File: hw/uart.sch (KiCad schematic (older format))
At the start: 0 parts

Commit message: hw: add MAX3109 symbol
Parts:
- added C?: 0.1, symbol C
- added C?: 1.0, symbol C
- added DD?: MAX3109, Housings_DFN_QFN:QFN-32-1EP_5x5mm_Pitch0.5mm, symbol MAX3109
- added R? (x2): 10k, symbol R
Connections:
- new net: DD?.1 (~RST), R?.1
- new net: C?.1, DD?.31 (V18)
- new net +3.3VP: C?.1, DD?.25 (Vext), DD?.30 (LDOEN), DD?.32 (Vcc), DD?.8 (Vl), DD?.9 (SPI/~I2C), R?.2, R?.2
- new net GND: C?.2, C?.2, DD?.10 (DGND), DD?.29 (AGND), DD?.33 (AGND)
- new net RPI_GPCLK0: DD?.26 (XIN)
- new net RPI_SPI0_MISO: DD?.2 (MISO/SDA)
- new net RPI_SPI0_MOSI: DD?.6 (MOSI/A1)
- new net RPI_SPI0_SCLK: DD?.3 (SCLK/SCL)
- new net ~RPI_SPI0_CE0: DD?.5 (~CS~/A0)
- new net ~SER_IRQ: DD?.7 (~IRQ), R?.1
- no-connect marks 0 -> 1
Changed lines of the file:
@@
 Comment4 ""
 $EndDescr
+$Comp
+L MAX3109 DD?
+U 1 1 5AB1B0A7
+P 4400 4900
+F 0 "DD?" H 3900 6100 60  0000 C CNN
+F 1 "MAX3109" H 4400 3700 60  0000 C CNN
+F 2 "Housings_DFN_QFN:QFN-32-1EP_5x5mm_Pitch0.5mm" H 4400 4600 60  0001 C CNN
+F 3 "" H 4400 4600 60  0001 C CNN
+	1    4400 4900
+	1    0    0    -1
+$EndComp
+$Comp
+L +3.3VP #PWR013
+U 1 1 5AB1B260
+P 3250 5400
+F 0 "#PWR013" H 3400 5350 50  0001 C CNN
+F 1 "+3.3VP" H 3250 5500 50  0000 C CNN
+F 2 "" H 3250 5400 50  0001 C CNN
+F 3 "" H 3250 5400 50  0001 C CNN
+	1    3250 5400
+	1    0    0    -1
+$EndComp
+$Comp
+L GND #PWR014
+U 1 1 5AB1B2D7
+P 3500 6500
+F 0 "#PWR014" H 3500 6250 50  0001 C CNN
+F 1 "GND" H 3500 6350 50  0000 C CNN
+F 2 "" H 3500 6500 50  0001 C CNN
+F 3 "" H 3500 6500 50  0001 C CNN
+	1    3500 6500
+	1    0    0    -1
+$EndComp
+NoConn ~ 3600 5150
+Text GLabel 2950 5050 0    60   Input ~ 0
+RPI_GPCLK0
+Wire Wire Line
+	2950 5050 3600 5050
+$Comp
+L C C?
+U 1 1 5AB1B470
+P 3250 6150
+F 0 "C?" H 3275 6250 50  0000 L CNN
+F 1 "0.1" H 3275 6050 50  0000 L CNN
+F 2 "" H 3288 6000 50  0001 C CNN
+F 3 "" H 3250 6150 50  0001 C CNN
+	1    3250 6150
+	1    0    0    -1
+$EndComp
+$Comp
+L C C?
+U 1 1 5AB1B4D8
+P 3500 6150
+F 0 "C?" H 3525 6250 50  0000 L CNN
+F 1 "1.0" H 3525 6050 50  0000 L CNN
+F 2 "" H 3538 6000 50  0001 C CNN
+F 3 "" H 3500 6150 50  0001 C CNN
+	1    3500 6150
+	1    0    0    -1
+$EndComp
+Wire Wire Line
+	3600 5900 3500 5900
+Wire Wire Line
+	3500 5900 3500 6000
+Wire Wire Line
+	3600 5500 3250 5500
+Wire Wire Line
+	3250 5400 3250 6000
+Wire Wire Line
+	3250 5600 3600 5600
+Connection ~ 3250 5600
+Wire Wire Line
+	3600 5700 3250 5700
+Connection ~ 3250 5700
+Connection ~ 3250 5500
+Wire Wire Line
+	3500 6300 3500 6500
+Wire Wire Line
+	3500 6400 3250 6400
+Wire Wire Line
+	3250 6400 3250 6300
+Connection ~ 3500 6400
+$Comp
+L +3.3VP #PWR015
+U 1 1 5AB1B914
+P 2900 4750
+F 0 "#PWR015" H 3050 4700 50  0001 C CNN
+F 1 "+3.3VP" H 2900 4850 50  0000 C CNN
+F 2 "" H 2900 4750 50  0001 C CNN
+F 3 "" H 2900 4750 50  0001 C CNN
+	1    2900 4750
+	0    -1   -1   0
+$EndComp
+$Comp
+L R R?
+U 1 1 5AB1B9A3
+P 3250 4550
+F 0 "R?" V 3330 4550 50  0000 C CNN
+F 1 "10k" V 3250 4550 50  0000 C CNN
+F 2 "" V 3180 4550 50  0001 C CNN
+F 3 "" H 3250 4550 50  0001 C CNN
+	1    3250 4550
+	0    1    1    0
+$EndComp
+Wire Wire Line
+	2900 4750 3600 4750
+Wire Wire Line
+	3600 4650 3500 4650
+Wire Wire Line
+	3500 4650 3500 4750
+Connection ~ 3500 4750
+Wire Wire Line
+	3000 4750 3000 4550
+Wire Wire Line
+	3000 4550 3100 4550
+Connection ~ 3000 4750
+Text GLabel 2950 4450 0    60   Output ~ 0
+~SER_IRQ
+Text GLabel 2950 4350 0    60   Input ~ 0
+~RPI_SPI0_CE0
+Text GLabel 2950 4250 0    60   Input ~ 0
+RPI_SPI0_SCLK
+Text GLabel 2950 4150 0    60   Input ~ 0
+RPI_SPI0_MOSI
+Text GLabel 2950 4050 0    60   Output ~ 0
+RPI_SPI0_MISO
+Wire Wire Line
+	2950 4050 3600 4050
+Wire Wire Line
+	3600 4150 2950 4150
+Wire Wire Line
+	2950 4250 3600 4250
+Wire Wire Line
+	3600 4350 2950 4350
+Wire Wire Line
+	2950 4450 3600 4450
+Wire Wire Line
+	3400 4550 3500 4550
+Wire Wire Line
+	3500 4550 3500 4450
+Connection ~ 3500 4450
+$Comp
+L GND #PWR016
+U 1 1 5AB1C686
+P 5300 6050
+F 0 "#PWR016" H 5300 5800 50  0001 C CNN
+F 1 "GND" H 5300 5900 50  0000 C CNN
+F 2 "" H 5300 6050 50  0001 C CNN
+F 3 "" H 5300 6050 50  0001 C CNN
+	1    5300 6050
+	1    0    0    -1
+$EndComp
+Wire Wire Line
+	5200 5700 5300 5700
+Wire Wire Line
+	5300 5700 5300 6050
+Wire Wire Line
+	5200 5800 5300 5800
+Connection ~ 5300 5800
+Wire Wire Line
+	5200 5900 5300 5900
+Connection ~ 5300 5900
+$Comp
+L R R?
+U 1 1 5AB1D90A
+P 3500 3650
+F 0 "R?" V 3580 3650 50  0000 C CNN
+F 1 "10k" V 3500 3650 50  0000 C CNN
+F 2 "" V 3430 3650 50  0001 C CNN
+F 3 "" H 3500 3650 50  0001 C CNN
+	1    3500 3650
+	-1   0    0    1
+$EndComp
+$Comp
+L +3.3VP #PWR017
+U 1 1 5AB1D959
+P 3500 3400
+F 0 "#PWR017" H 3650 3350 50  0001 C CNN
+F 1 "+3.3VP" H 3500 3500 50  0000 C CNN
+F 2 "" H 3500 3400 50  0001 C CNN
+F 3 "" H 3500 3400 50  0001 C CNN
+	1    3500 3400
+	1    0    0    -1
+$EndComp
+Wire Wire Line
+	3600 3900 3500 3900
+Wire Wire Line
+	3500 3900 3500 3800
+Wire Wire Line
+	3500 3500 3500 3400
 $EndSCHEMATC

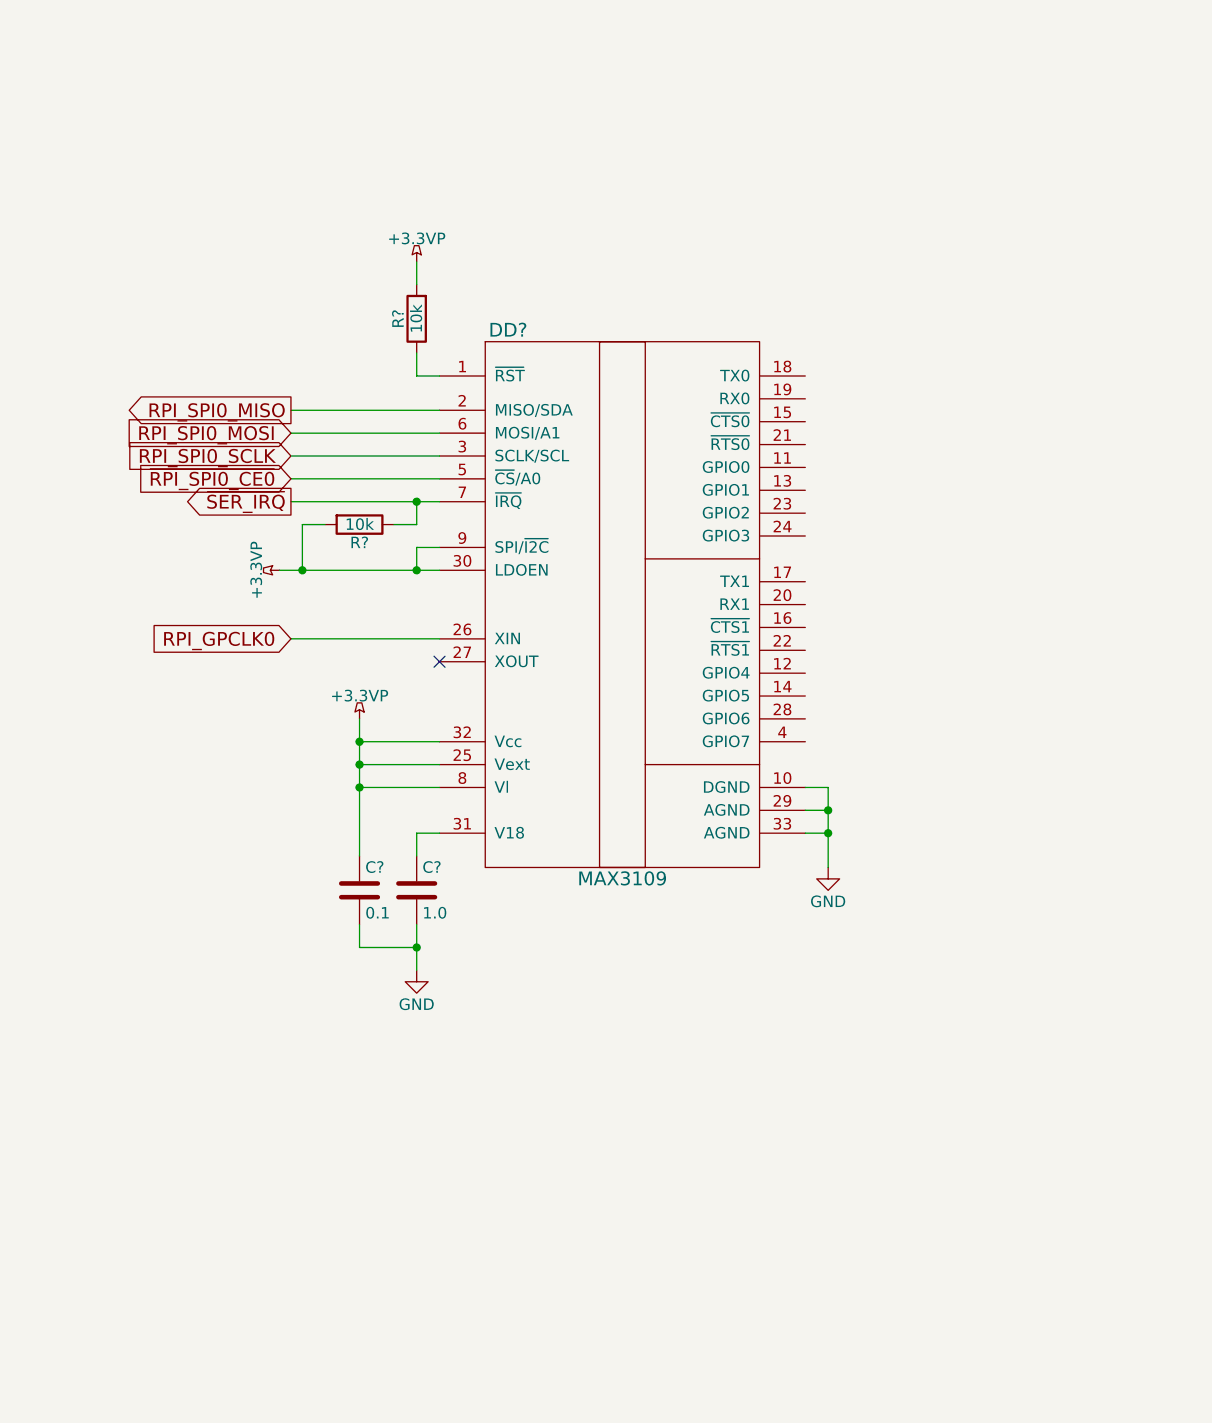
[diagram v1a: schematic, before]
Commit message: hw: add uart conns
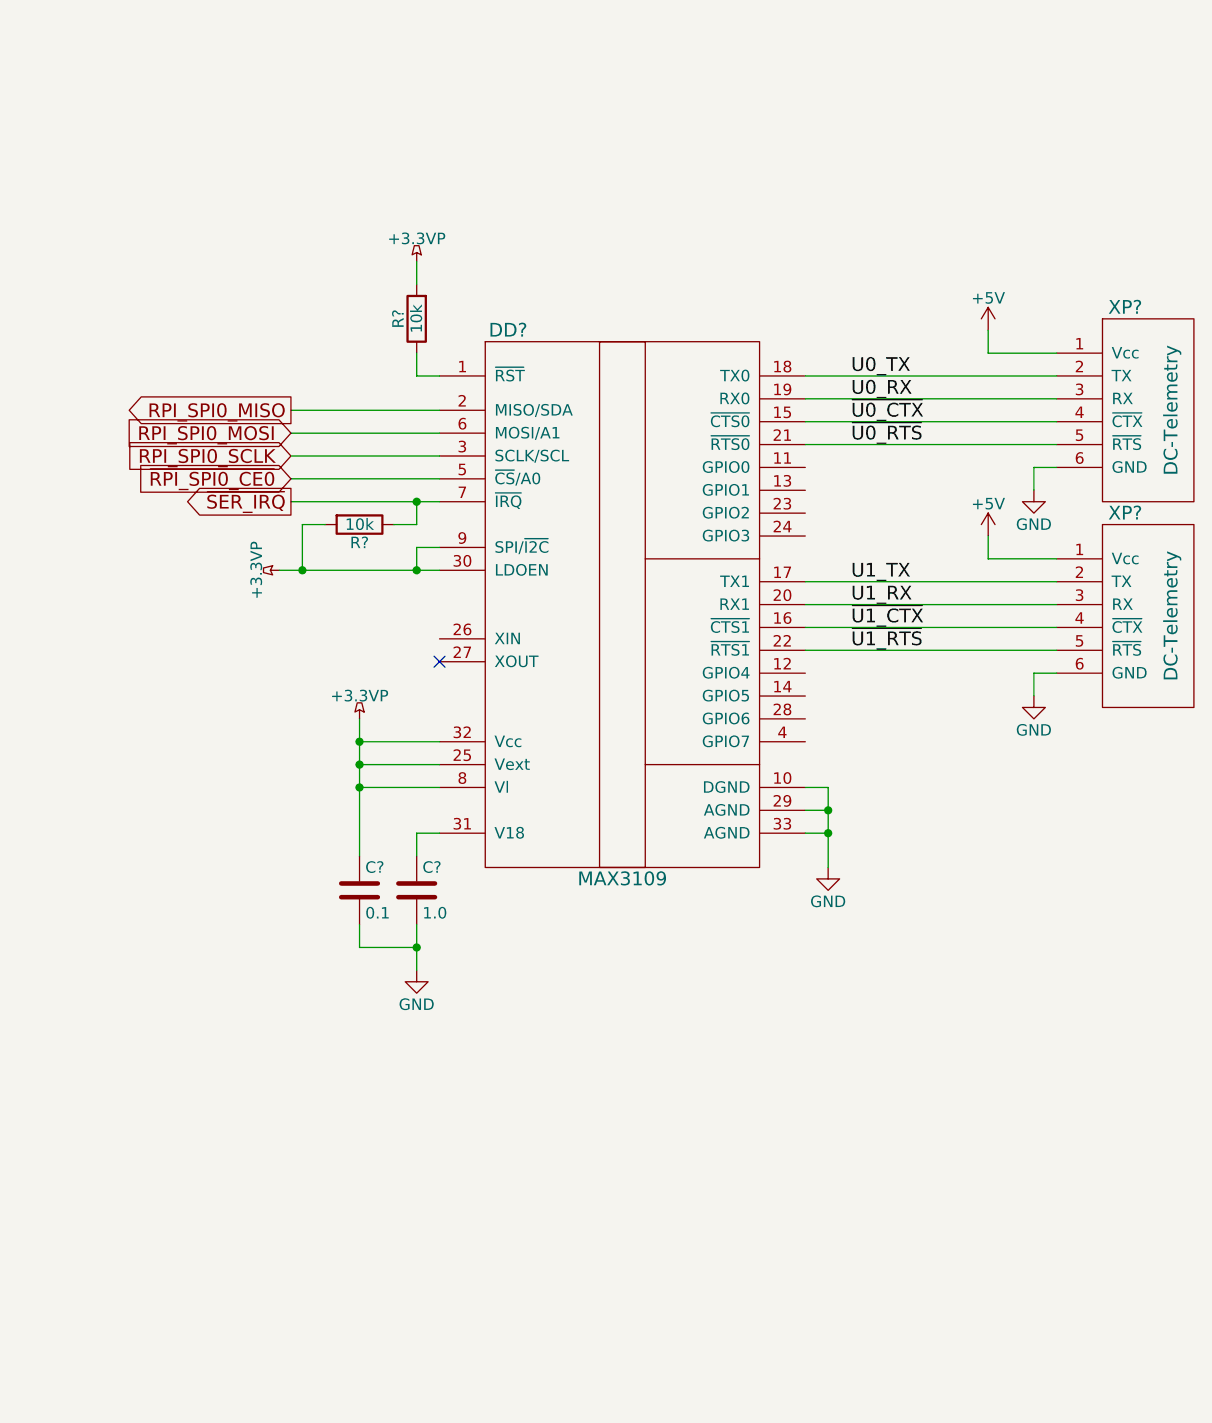
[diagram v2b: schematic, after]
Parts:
- added XP? (x2): DC-Telemetry, symbol DC-Telemetry
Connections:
- net GND: now also XP?.6 (GND), XP?.6 (GND)
- net ~U0_CTX: now reaches DD?.15 (~CTS0)
- net ~U0_CTX: now also XP?.4 (~CTX)
- net ~U1_CTX: now reaches DD?.16 (~CTS1)
- net ~U1_CTX: now also XP?.4 (~CTX)
- net U1_TX: now reaches DD?.17 (TX1)
- net U1_TX: now also XP?.2 (TX)
- net U0_TX: now reaches DD?.18 (TX0)
- net U0_TX: now also XP?.2 (TX)
- net U0_RX: now reaches DD?.19 (RX0)
- net U0_RX: now also XP?.3 (RX)
- net U1_RX: now reaches DD?.20 (RX1)
- net U1_RX: now also XP?.3 (RX)
- net ~U0_RTS: now reaches DD?.21 (~RTS0)
- net ~U0_RTS: now also XP?.5 (~RTS)
- net ~U1_RTS: now reaches DD?.22 (~RTS1)
- net ~U1_RTS: now also XP?.5 (~RTS)
- net RPI_GPCLK0: no longer names the net of DD?.26 (XIN)
- new net +5V: XP?.1 (Vcc), XP?.1 (Vcc)
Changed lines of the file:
@@
 LIBS:rpi_con
 LIBS:ic
+LIBS:dronecode_con
 LIBS:obc-drone-hat-cache
 EELAYER 25 0
@@
 $EndComp
 NoConn ~ 3600 5150
-Text GLabel 2950 5050 0    60   Input ~ 0
-RPI_GPCLK0
-Wire Wire Line
-	2950 5050 3600 5050
 $Comp
 L C C?
@@
 	3600 5500 3250 5500
 Wire Wire Line
-	3250 5400 3250 6000
+	3250 5400 3250 5500
+Wire Wire Line
+	3250 5500 3250 5600
+Wire Wire Line
+	3250 5600 3250 5700
+Wire Wire Line
+	3250 5700 3250 6000
 Wire Wire Line
 	3250 5600 3600 5600
@@
 Connection ~ 3250 5500
 Wire Wire Line
-	3500 6300 3500 6500
+	3500 6300 3500 6400
+Wire Wire Line
+	3500 6400 3500 6500
 Wire Wire Line
 	3500 6400 3250 6400
@@
 $EndComp
 Wire Wire Line
-	2900 4750 3600 4750
+	2900 4750 3000 4750
+Wire Wire Line
+	3000 4750 3500 4750
+Wire Wire Line
+	3500 4750 3600 4750
 Wire Wire Line
 	3600 4650 3500 4650
@@
 	3600 4350 2950 4350
 Wire Wire Line
-	2950 4450 3600 4450
+	2950 4450 3500 4450
+Wire Wire Line
+	3500 4450 3600 4450
 Wire Wire Line
 	3400 4550 3500 4550
@@
 L GND #PWR016
 U 1 1 5AB1C686
-P 5300 6050
-F 0 "#PWR016" H 5300 5800 50  0001 C CNN
-F 1 "GND" H 5300 5900 50  0000 C CNN
-F 2 "" H 5300 6050 50  0001 C CNN
-F 3 "" H 5300 6050 50  0001 C CNN
-	1    5300 6050
+P 6200 4400
+F 0 "#PWR016" H 6200 4150 50  0001 C CNN
+F 1 "GND" H 6200 4250 50  0000 C CNN
+F 2 "" H 6200 4400 50  0001 C CNN
+F 3 "" H 6200 4400 50  0001 C CNN
+	1    6200 4400
 	1    0    0    -1
 $EndComp
@@
 	5200 5700 5300 5700
 Wire Wire Line
-	5300 5700 5300 6050
+	5300 5700 5300 5800
+Wire Wire Line
+	5300 5800 5300 5900
+Wire Wire Line
+	5300 5900 5300 6050
 Wire Wire Line
 	5200 5800 5300 5800
@@
 Wire Wire Line
 	3500 3500 3500 3400
+$Comp
+L DC-Telemetry XP?
+U 1 1 5AB2FA79
+P 6700 4050
+F 0 "XP?" H 6600 4500 60  0000 C CNN
+F 1 "DC-Telemetry" V 6800 4050 60  0000 C CNN
+F 2 "" H 6700 4050 60  0001 C CNN
+F 3 "" H 6700 4050 60  0001 C CNN
+	1    6700 4050
+	1    0    0    -1
+$EndComp
+$Comp
+L DC-Telemetry XP?
+U 1 1 5AB2FFF0
+P 6700 4950
+F 0 "XP?" H 6600 5400 60  0000 C CNN
+F 1 "DC-Telemetry" V 6800 4950 60  0000 C CNN
+F 2 "" H 6700 4950 60  0001 C CNN
+F 3 "" H 6700 4950 60  0001 C CNN
+	1    6700 4950
+	1    0    0    -1
+$EndComp
+Wire Wire Line
+	5200 3900 6300 3900
+Wire Wire Line
+	5200 4000 6300 4000
+Wire Wire Line
+	5200 4800 6300 4800
+Wire Wire Line
+	6300 4900 5200 4900
+Wire Wire Line
+	5200 4100 6300 4100
+Wire Wire Line
+	5200 4200 6300 4200
+Wire Wire Line
+	5200 5000 6300 5000
+Wire Wire Line
+	6300 5100 5200 5100
+$Comp
+L +5V #PWR?
+U 1 1 5AB3063A
+P 6000 3700
+F 0 "#PWR?" H 6000 3550 50  0001 C CNN
+F 1 "+5V" H 6000 3840 50  0000 C CNN
+F 2 "" H 6000 3700 50  0001 C CNN
+F 3 "" H 6000 3700 50  0001 C CNN
+	1    6000 3700
+	1    0    0    -1
+$EndComp
+Wire Wire Line
+	6300 4300 6200 4300
+Wire Wire Line
+	6200 4300 6200 4400
+$Comp
+L GND #PWR?
+U 1 1 5AB30BD8
+P 5300 6050
+F 0 "#PWR?" H 5300 5800 50  0001 C CNN
+F 1 "GND" H 5300 5900 50  0000 C CNN
+F 2 "" H 5300 6050 50  0001 C CNN
+F 3 "" H 5300 6050 50  0001 C CNN
+	1    5300 6050
+	1    0    0    -1
+$EndComp
+$Comp
+L GND #PWR?
+U 1 1 5AB30BF8
+P 6200 5300
+F 0 "#PWR?" H 6200 5050 50  0001 C CNN
+F 1 "GND" H 6200 5150 50  0000 C CNN
+F 2 "" H 6200 5300 50  0001 C CNN
+F 3 "" H 6200 5300 50  0001 C CNN
+	1    6200 5300
+	1    0    0    -1
+$EndComp
+$Comp
+L +5V #PWR?
+U 1 1 5AB30E1E
+P 6000 4600
+F 0 "#PWR?" H 6000 4450 50  0001 C CNN
+F 1 "+5V" H 6000 4740 50  0000 C CNN
+F 2 "" H 6000 4600 50  0001 C CNN
+F 3 "" H 6000 4600 50  0001 C CNN
+	1    6000 4600
+	1    0    0    -1
+$EndComp
+Wire Wire Line
+	6300 5200 6200 5200
+Wire Wire Line
+	6200 5200 6200 5300
+Wire Wire Line
+	6300 4700 6000 4700
+Wire Wire Line
+	6000 4700 6000 4600
+Wire Wire Line
+	6300 3800 6000 3800
+Wire Wire Line
+	6000 3800 6000 3700
+Text Label 5400 3900 0    60   ~ 0
+U0_TX
+Text Label 5400 4000 0    60   ~ 0
+U0_RX
+Text Label 5400 4100 0    60   ~ 0
+~U0_CTX
+Text Label 5400 4200 0    60   ~ 0
+~U0_RTS
+Text Label 5400 4800 0    60   ~ 0
+U1_TX
+Text Label 5400 4900 0    60   ~ 0
+U1_RX
+Text Label 5400 5000 0    60   ~ 0
+~U1_CTX
+Text Label 5400 5100 0    60   ~ 0
+~U1_RTS
 $EndSCHEMATC

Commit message: hw: add fallback clk source
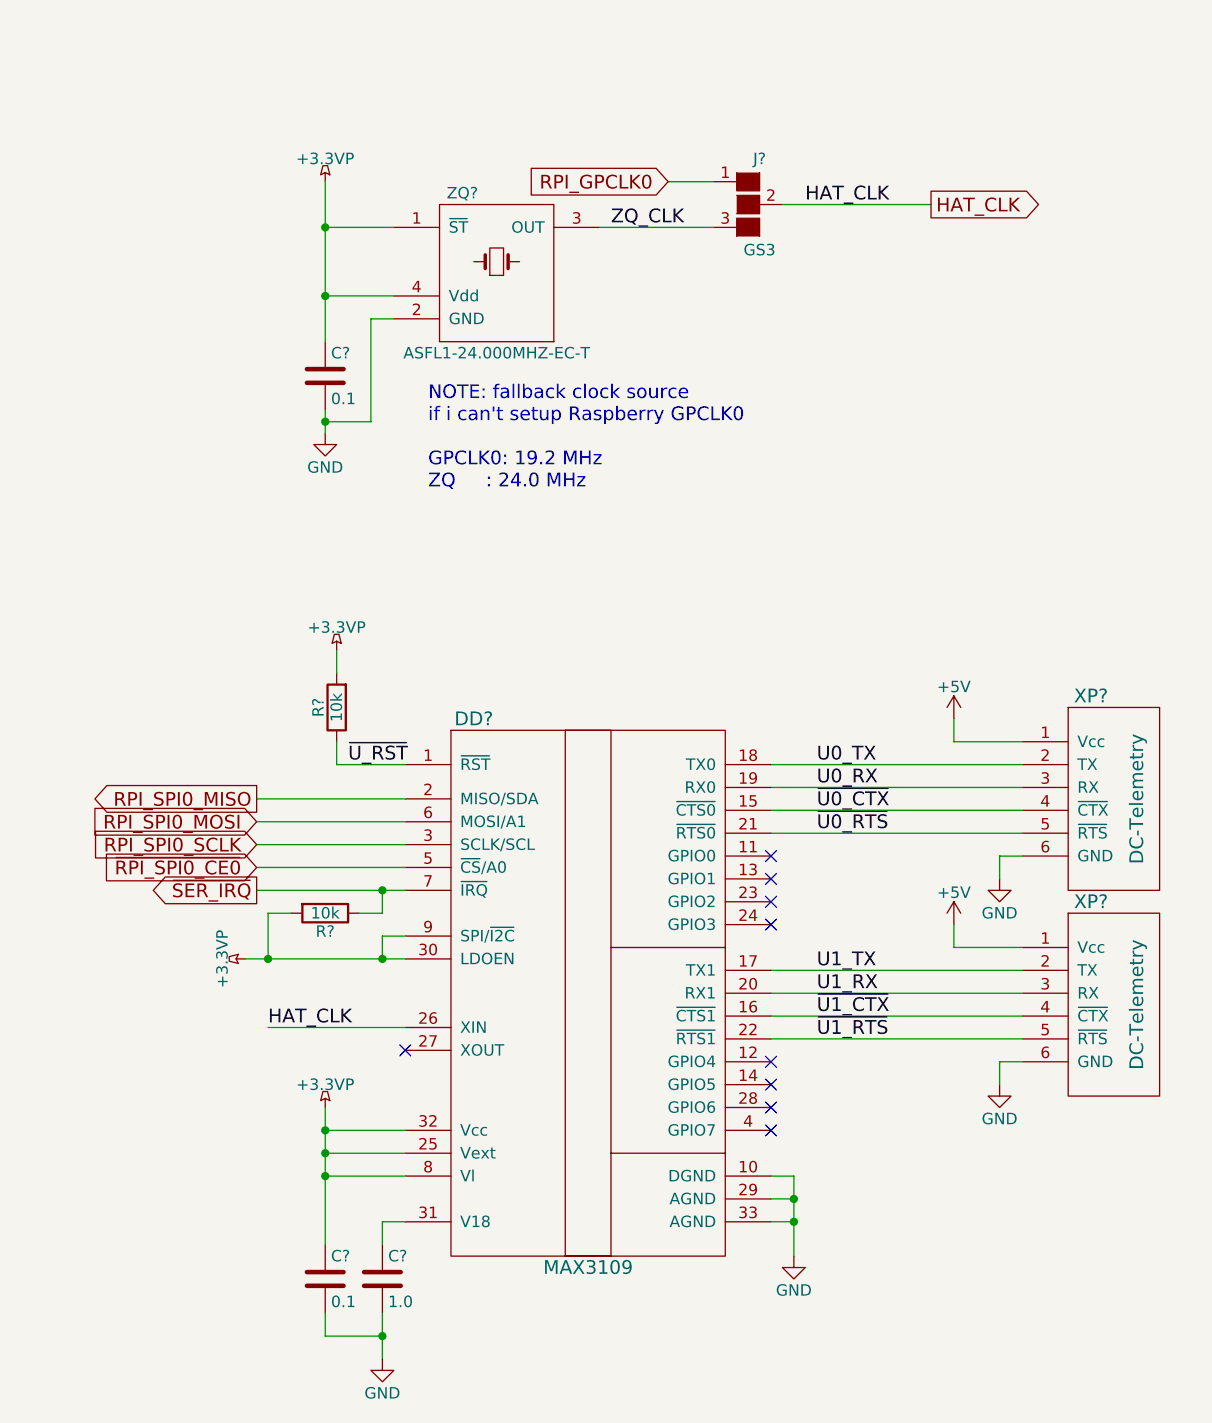
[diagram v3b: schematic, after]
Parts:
- added C?: 0.1, symbol C
- added J?: GS3, Connectors:GS3, symbol GS3
- added ZQ?: ASFL1-24.000MHZ-EC-T, Crystals:Crystal_SMD_Abracon_ABM3B-4pin_5.0x3.2mm, symbol ASFL1
- XP? (x2): footprint (none) -> Connectors_JST:JST_GH_SM06B-GHS-TB_06x1.25mm_Angled
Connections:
- net +3.3VP: now also C?.1, ZQ?.1 (~ST), ZQ?.4 (Vdd)
- net GND: now also C?.2, ZQ?.2 (GND)
- net ~U_RST: now reaches DD?.1 (~RST), R?.1
- net HAT_CLK: now reaches DD?.26 (XIN)
- net HAT_CLK: now also J?.2 (G2)
- new net RPI_GPCLK0: J?.1 (G1)
- new net ZQ_CLK: J?.3 (G3), ZQ?.3 (OUT)
- no-connect marks 1 -> 9
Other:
- note added: "NOTE: fallback clock source\nif i can't setup Raspberry GPCLK0\n\nGPCLK0: 19.2 MHz\nZQ : 24.0 MHz"
- moved on the sheet: C?, DD?, R?, XP?
